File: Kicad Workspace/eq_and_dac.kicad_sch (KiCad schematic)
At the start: 2 parts, among them U3 PCM5242RHBT, U4 TMUX1574PW

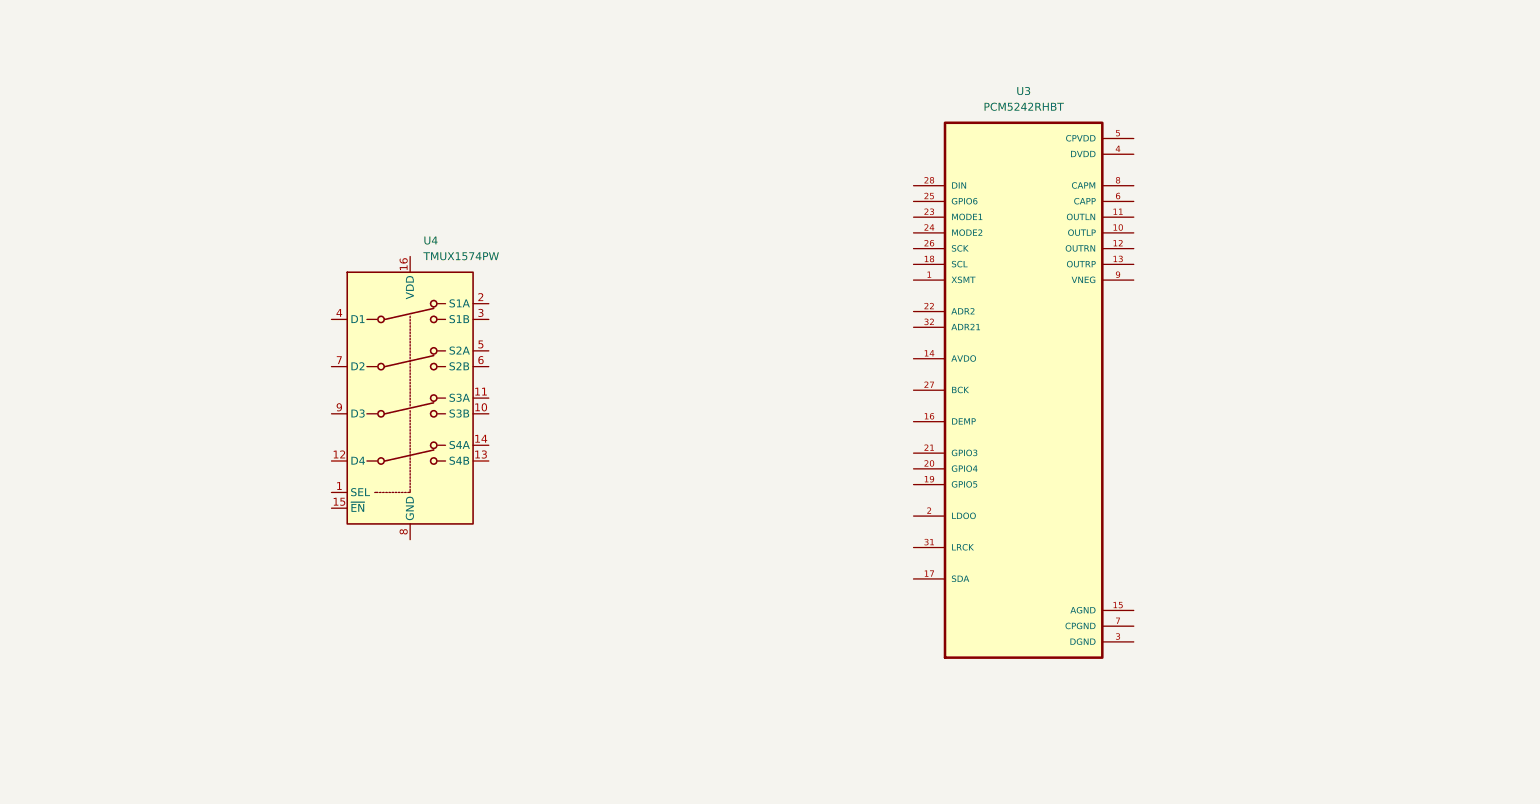
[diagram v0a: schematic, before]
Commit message: feat: MUX + DAC Kicad schematics done
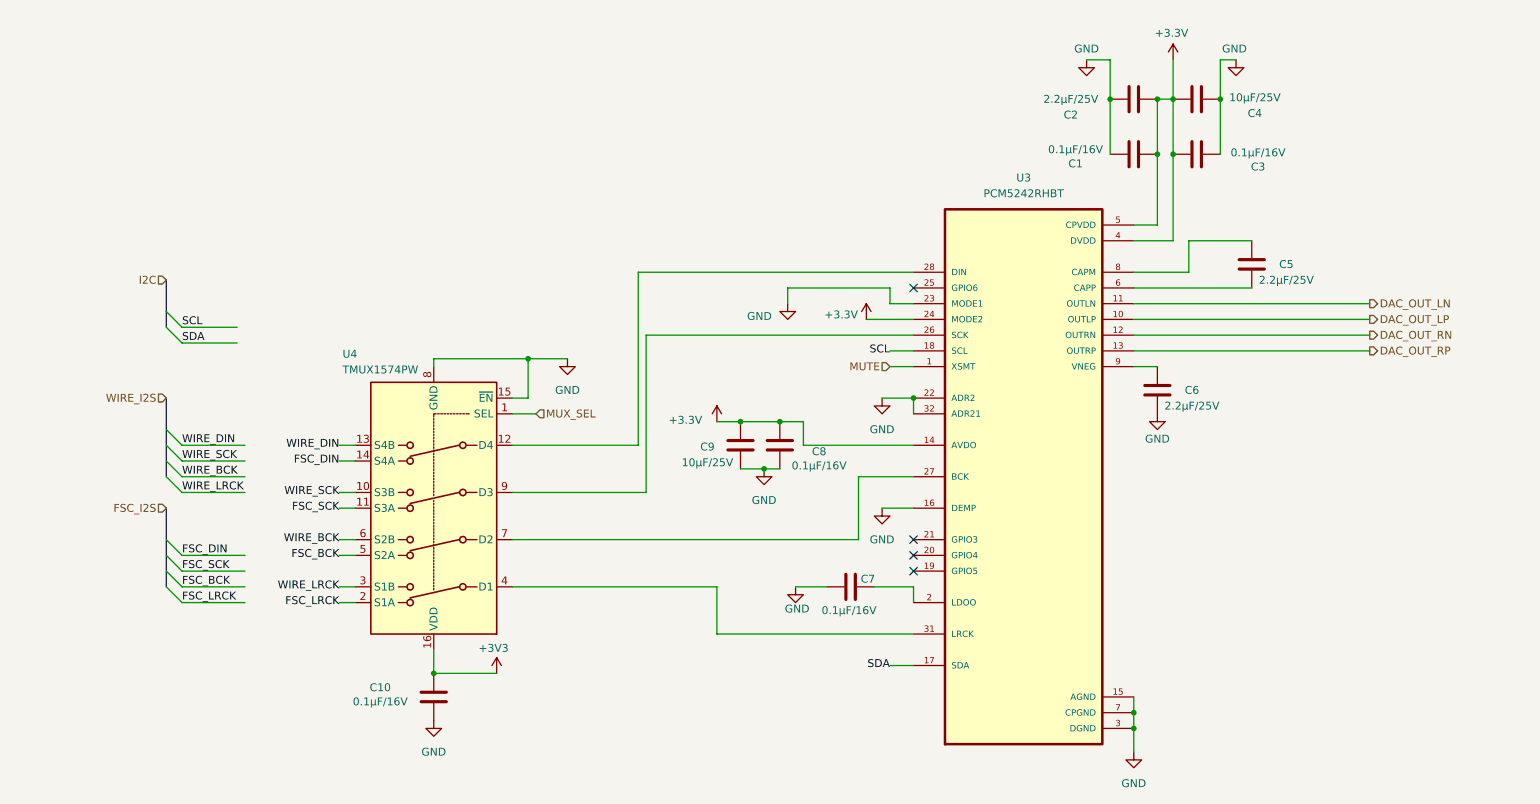
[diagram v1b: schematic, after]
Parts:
- added C1, C10, C3, C7, C8: 0.1µF/16V, Capacitor_SMD:C_0402_1005Metric, symbol Device:C
- added C2, C5, C6: 2.2µF/25V, Capacitor_SMD:C_0805_2012Metric, symbol Device:C
- added C4, C9: 10µF/25V, Capacitor_SMD:C_0805_2012Metric, symbol Device:C
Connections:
- net MUX_SEL: now reaches U4.1 (SEL)
- net WIRE_SCK: now reaches U4.10 (S3B)
- net FSC_SCK: now reaches U4.11 (S3A)
- net at U4.12 (D4): now also U3.28 (DIN)
- net WIRE_DIN: now reaches U4.13 (S4B)
- net FSC_DIN: now reaches U4.14 (S4A)
- net GND: now reaches U4.15 (~{EN})
- net GND: now also U3.15 (AGND), U3.16 (DEMP), U3.22 (ADR2), U3.23 (MODE1), U3.3 (DGND), U3.32 (ADR21), U3.7 (CPGND), U4.8 (GND), C1.1, C10.1, C2.1, C3.2, C4.2, C6.2, C7.1, C8.1, C9.1
- net +3V3: now reaches U4.16 (VDD)
- net +3V3: now also C10.2
- net FSC_LRCK: now reaches U4.2 (S1A)
- net WIRE_LRCK: now reaches U4.3 (S1B)
- net at U4.4 (D1): now also U3.31 (LRCK)
- net FSC_BCK: now reaches U4.5 (S2A)
- net WIRE_BCK: now reaches U4.6 (S2B)
- net at U4.7 (D2): now also U3.27 (BCK)
- net at U4.9 (D3): now also U3.26 (SCK)
- net MUTE: now reaches U3.1 (XSMT)
- net DAC_OUT_LP: now reaches U3.10 (OUTLP)
- net DAC_OUT_LN: now reaches U3.11 (OUTLN)
- net DAC_OUT_RN: now reaches U3.12 (OUTRN)
- net DAC_OUT_RP: now reaches U3.13 (OUTRP)
- net +3.3V: now reaches U3.14 (AVDO)
- net +3.3V: now also U3.24 (MODE2), U3.4 (DVDD), U3.5 (CPVDD), C1.2, C2.2, C3.1, C4.1, C8.2, C9.2
- net SDA: now reaches U3.17 (SDA)
- net SCL: now reaches U3.18 (SCL)
- net at U3.2 (LDOO): now also C7.2
- net at U3.6 (CAPP): now also C5.2
- net at U3.8 (CAPM): now also C5.1
- net at U3.9 (VNEG): now also C6.1
- no-connect marks 0 -> 4
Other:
- moved on the sheet: U3, U4

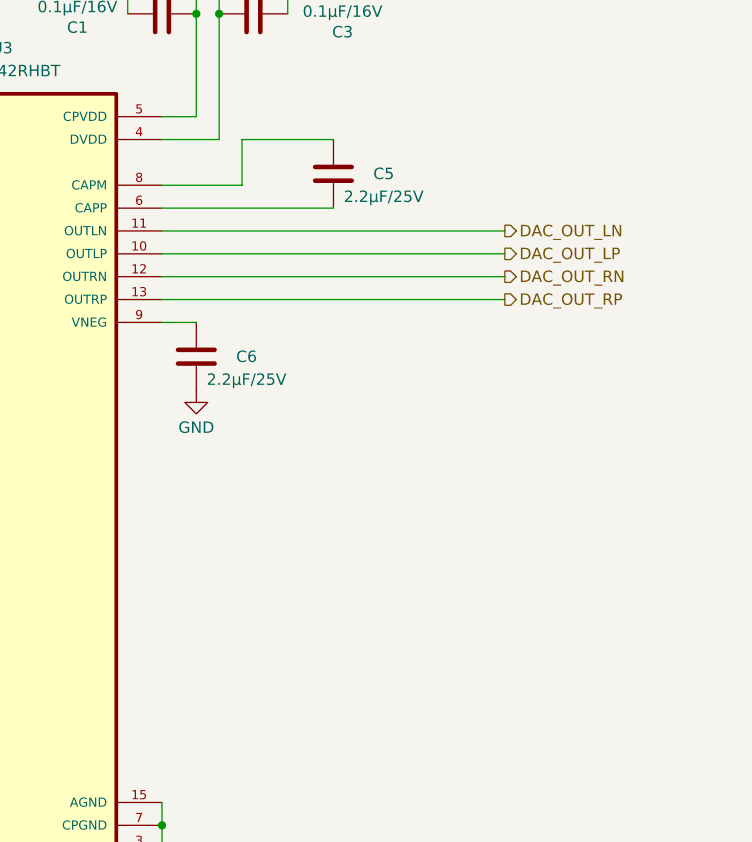
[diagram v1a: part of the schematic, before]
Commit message: feat: filtering analog output
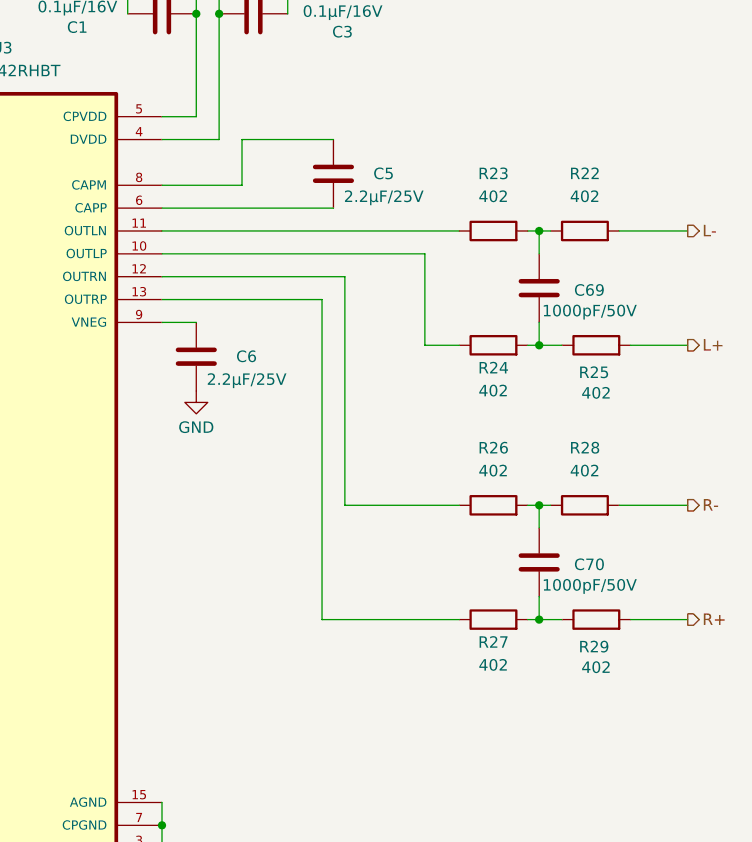
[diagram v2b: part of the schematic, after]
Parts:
- added C69, C70: 1000pF/50V, Capacitor_SMD:C_0201_0603Metric, symbol Device:C
- added R22, R23, R24, R25, R26, R27, R28, R29: 402, Resistor_SMD:R_0201_0603Metric, symbol Device:R
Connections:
- net DAC_OUT_LN: no longer names the net of U3.11 (OUTLN)
- net DAC_OUT_LN: now also R23.1
- net DAC_OUT_LP: no longer names the net of U3.10 (OUTLP)
- net DAC_OUT_LP: now also R24.1
- net DAC_OUT_RN: no longer names the net of U3.12 (OUTRN)
- net DAC_OUT_RN: now also R26.1
- net DAC_OUT_RP: no longer names the net of U3.13 (OUTRP)
- net DAC_OUT_RP: now also R27.1
- new net: C69.2, R22.1, R23.2
- new net: C70.2, R26.2, R28.1
- new net: C69.1, R24.2, R25.1
- new net: C70.1, R27.2, R29.1
- new net L+: R25.2
- new net L-: R22.2
- new net R+: R29.2
- new net R-: R28.2

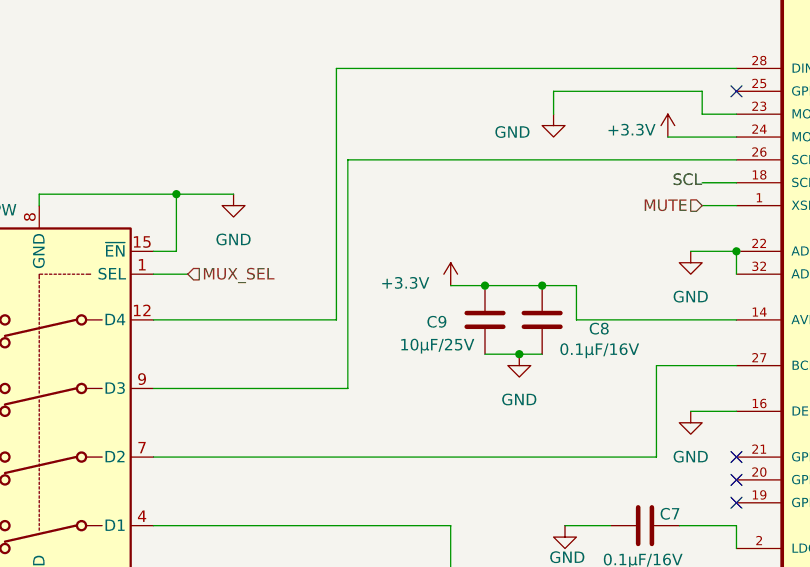
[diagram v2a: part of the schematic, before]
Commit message: fix: split analog 3.3 from digital 3.3
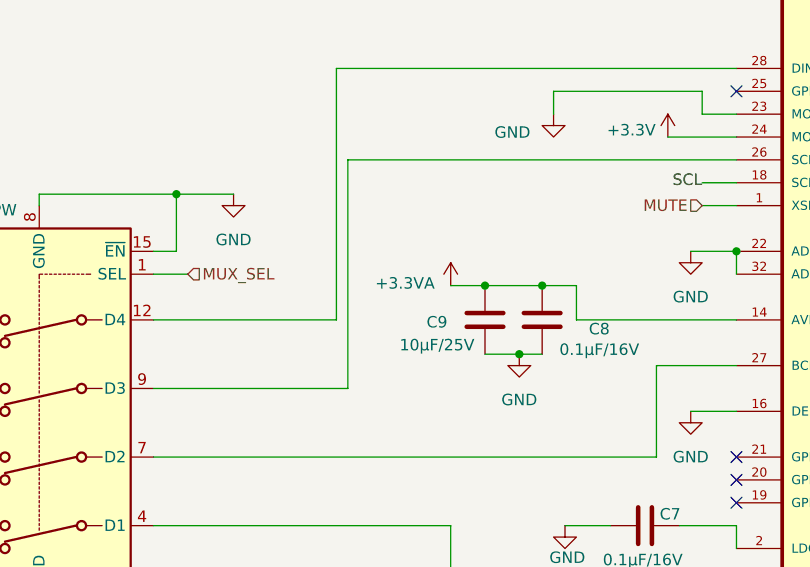
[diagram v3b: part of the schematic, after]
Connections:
- net +3.3V: no longer C8.2, C9.2, U3.14 (AVDO)
- new net +3.3VA: C8.2, C9.2, U3.14 (AVDO)
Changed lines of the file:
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@@
 			)
 		)
-		(property "Value" "+3.3V"
+		(property "Value" "+3.3VA"
 			(at 130.81 93.726 0)
 			(show_name no)

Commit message: feat: schematics almost done, starting to correct compile pb
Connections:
- net FSC_SCK is gone; now on net GND: U4.11 (S3A)
- net WIRE_SCK is gone; now on net GND: U4.10 (S3B)
- net GND: now also U3.26 (SCK), U4.9 (D3)
- net FSC_BCK renamed BT_BCK
- net FSC_DIN renamed BT_DATA
- net FSC_LRCK renamed BT_LRCK
- net WIRE_DIN renamed WIRE_DATA

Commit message: feat: correction work in progress
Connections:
- net SCL renamed I2S.SCL
- net SDA renamed I2S.SDA
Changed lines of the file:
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@@
 	)
 	(bus_entry
-		(at 95.25 54.61)
+		(at 73.66 52.07)
 		(size 2.54 2.54)
 		(stroke
@@
 	)
 	(bus_entry
-		(at 95.25 69.85)
+		(at 73.66 67.31)
 		(size 2.54 2.54)
 		(stroke
@@
 	)
 	(bus_entry
-		(at 95.25 52.07)
+		(at 73.66 49.53)
 		(size 2.54 2.54)
 		(stroke
@@
 	)
 	(bus_entry
-		(at 95.25 72.39)
+		(at 73.66 69.85)
 		(size 2.54 2.54)
 		(stroke
@@
 	)
 	(bus_entry
-		(at 95.25 67.31)
+		(at 73.66 64.77)
 		(size 2.54 2.54)
 		(stroke
@@
 	)
 	(bus_entry
-		(at 95.25 49.53)
+		(at 73.66 46.99)
 		(size 2.54 2.54)
 		(stroke
@@
 	(wire
 		(pts
-			(xy 97.79 72.39) (xy 107.95 72.39)
+			(xy 76.2 69.85) (xy 86.36 69.85)
 		)
 		(stroke
@@
 	(wire
 		(pts
-			(xy 97.79 57.15) (xy 107.95 57.15)
+			(xy 76.2 54.61) (xy 86.36 54.61)
 		)
 		(stroke
@@
 	(wire
 		(pts
-			(xy 97.79 52.07) (xy 107.95 52.07)
-		)
-		(stroke
-			(width 0)
-			(type default)
-		)
-	)
-	(wire
-		(pts
-			(xy 97.79 69.85) (xy 107.95 69.85)
+			(xy 76.2 49.53) (xy 86.36 49.53)
+		)
+		(stroke
+			(width 0)
+			(type default)
+		)
+	)
+	(wire
+		(pts
+			(xy 76.2 67.31) (xy 86.36 67.31)
 		)
 		(stroke
@@
 	(wire
 		(pts
-			(xy 97.79 54.61) (xy 107.95 54.61)
+			(xy 76.2 52.07) (xy 86.36 52.07)
 		)
 		(stroke
@@
 	(wire
 		(pts
-			(xy 97.79 74.93) (xy 107.95 74.93)
+			(xy 76.2 72.39) (xy 86.36 72.39)
 		)
 		(stroke
@@
 	(bus
 		(pts
-			(xy 95.25 59.69) (xy 95.25 72.39)
+			(xy 73.66 57.15) (xy 73.66 69.85)
 		)
 		(stroke
@@
 	(bus
 		(pts
-			(xy 95.25 41.91) (xy 95.25 54.61)
+			(xy 73.66 39.37) (xy 73.66 52.07)
 		)
 		(stroke
@@
 		)
 	)
-	(label "SDA"
+	(label "WIRE_LRCK"
+		(at 86.36 54.61 0)
+		(effects
+			(font
+				(size 1.27 1.27)
+				(thickness 0.1588)
+			)
+			(justify left bottom)
+		)
+	)
+	(label "I2S.SDA"
 		(at 163.83 133.35 180)
 		(effects
@@
 		)
 	)
-	(label "WIRE_LRCK"
-		(at 97.79 57.15 0)
-		(effects
-			(font
-				(size 1.27 1.27)
-				(thickness 0.1588)
-			)
-			(justify left bottom)
-		)
-	)
 	(label "BT_LRCK"
 		(at 74.93 123.19 180)
@@
 		)
 	)
-	(label "WIRE_BCK"
-		(at 97.79 54.61 0)
+	(label "BT_BCK"
+		(at 76.2 69.85 0)
 		(effects
 			(font
@@
 		)
 	)
-	(label "BT_BCK"
-		(at 97.79 72.39 0)
-		(effects
-			(font
-				(size 1.27 1.27)
-				(thickness 0.1588)
-			)
-			(justify left bottom)
-		)
-	)
-	(label "SDA"
+	(label "I2S.SDA"
 		(at 127 40.64 180)
 		(effects
@@
 		)
 	)
-	(label "SCL"
+	(label "WIRE_DATA"
+		(at 86.36 49.53 0)
+		(effects
+			(font
+				(size 1.27 1.27)
+				(thickness 0.1588)
+			)
+			(justify left bottom)
+		)
+	)
+	(label "I2S.SCL"
 		(at 163.83 82.55 180)
 		(effects
@@
 		)
 	)
+	(label "WIRE_BCK"
+		(at 86.36 52.07 0)
+		(effects
+			(font
+				(size 1.27 1.27)
+				(thickness 0.1588)
+			)
+			(justify left bottom)
+		)
+	)
 	(label "BT_DATA"
-		(at 97.79 69.85 0)
+		(at 76.2 67.31 0)
 		(effects
 			(font
@@
 		)
 	)
-	(label "WIRE_DATA"
-		(at 97.79 52.07 0)
+	(label "BT_LRCK"
+		(at 76.2 72.39 0)
 		(effects
 			(font
@@
 		)
 	)
-	(label "BT_LRCK"
-		(at 97.79 74.93 0)
-		(effects
-			(font
-				(size 1.27 1.27)
-				(thickness 0.1588)
-			)
-			(justify left bottom)
-		)
-	)
-	(label "SCL"
+	(label "I2S.SCL"
 		(at 127 36.83 180)
 		(effects
@@
 	(hierarchical_label "WIRE_I2S{WIRE_DATA WIRE_BCK WIRE_LRCK}"
 		(shape input)
-		(at 95.25 41.91 180)
+		(at 73.66 39.37 180)
 		(effects
 			(font
@@
 	(hierarchical_label "BT_I2S{BT_DATA BT_BCK BT_LRCK}"
 		(shape input)
-		(at 95.25 59.69 180)
-		(effects
-			(font
+		(at 73.66 57.15 180)
+		(effects
+			(font

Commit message: project update
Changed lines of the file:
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@@
 		(property "Footprint" "PCM5242RHBT:IC_ADS125H01IRHBT"
 			(at 185.42 102.87 0)
-			(hide yes)
 			(show_name no)
 			(do_not_autoplace no)

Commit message: fix: Bus fix with correct syntax
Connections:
- net +3V3 is gone; now on net +3.3V: C10.2, U4.16 (VDD)
- net BT_BCK renamed BT_I2S.BCK
- net BT_DATA renamed BT_I2S.DATA
- net BT_LRCK renamed BT_I2S.LRCK
- net I2S.SCL renamed I2C.SCL
- net I2S.SDA renamed I2C.SDA
- net WIRE_BCK renamed WIRE_I2S.BCK
- net WIRE_DATA renamed WIRE_I2S.DATA
- net WIRE_LRCK renamed WIRE_I2S.LRCK
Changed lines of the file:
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@@
 	(wire
 		(pts
-			(xy 76.2 69.85) (xy 86.36 69.85)
-		)
-		(stroke
-			(width 0)
-			(type default)
-		)
-	)
-	(wire
-		(pts
 			(xy 245.11 74.93) (xy 246.38 74.93)
 		)
@@
 	(wire
 		(pts
-			(xy 76.2 49.53) (xy 86.36 49.53)
-		)
-		(stroke
-			(width 0)
-			(type default)
-		)
-	)
-	(wire
-		(pts
 			(xy 76.2 67.31) (xy 86.36 67.31)
 		)
@@
 	(wire
 		(pts
+			(xy 76.2 69.85) (xy 86.36 69.85)
+		)
+		(stroke
+			(width 0)
+			(type default)
+		)
+	)
+	(wire
+		(pts
 			(xy 74.93 113.03) (xy 77.47 113.03)
 		)
@@
 	(wire
 		(pts
+			(xy 76.2 49.53) (xy 86.36 49.53)
+		)
+		(stroke
+			(width 0)
+			(type default)
+		)
+	)
+	(wire
+		(pts
 			(xy 245.11 105.41) (xy 245.11 107.95)
 		)
@@
 	(wire
 		(pts
-			(xy 76.2 72.39) (xy 86.36 72.39)
+			(xy 254 74.93) (xy 261.62 74.93)
 		)
 		(stroke
@@
 	(wire
 		(pts
-			(xy 254 74.93) (xy 261.62 74.93)
+			(xy 217.17 35.56) (xy 217.17 41.91)
 		)
 		(stroke
@@
 	(wire
 		(pts
-			(xy 217.17 35.56) (xy 217.17 41.91)
+			(xy 254 105.41) (xy 261.62 105.41)
 		)
 		(stroke
@@
 	(wire
 		(pts
-			(xy 254 105.41) (xy 261.62 105.41)
+			(xy 232.41 87.63) (xy 236.22 87.63)
 		)
 		(stroke
@@
 	(wire
 		(pts
-			(xy 232.41 87.63) (xy 236.22 87.63)
+			(xy 76.2 72.39) (xy 86.36 72.39)
 		)
 		(stroke
@@
 		)
 	)
-	(label "WIRE_LRCK"
+	(label "WIRE_I2S.LRCK"
 		(at 86.36 54.61 0)
 		(effects
@@
 		)
 	)
-	(label "I2S.SDA"
+	(label "I2C.SDA"
 		(at 163.83 133.35 180)
 		(effects
@@
 		)
 	)
-	(label "BT_BCK"
+	(label "BT_I2S.BCK"
 		(at 74.93 115.57 180)
 		(effects
@@
 		)
 	)
-	(label "BT_LRCK"
+	(label "BT_I2S.LRCK"
 		(at 74.93 123.19 180)
 		(effects
@@
 		)
 	)
-	(label "BT_BCK"
-		(at 76.2 69.85 0)
+	(label "BT_I2S.BCK"
+		(at 86.36 69.85 0)
 		(effects
 			(font
@@
 		)
 	)
-	(label "I2S.SDA"
+	(label "I2C.SDA"
 		(at 127 40.64 180)
 		(effects
@@
 		)
 	)
-	(label "WIRE_DATA"
+	(label "WIRE_I2S.DATA"
 		(at 74.93 97.79 180)
 		(effects
@@
 		)
 	)
-	(label "WIRE_DATA"
+	(label "WIRE_I2S.DATA"
 		(at 86.36 49.53 0)
 		(effects
@@
 		)
 	)
-	(label "I2S.SCL"
+	(label "I2C.SCL"
 		(at 163.83 82.55 180)
 		(effects
@@
 		)
 	)
-	(label "WIRE_LRCK"
+	(label "WIRE_I2S.LRCK"
 		(at 74.93 120.65 180)
 		(effects
@@
 		)
 	)
-	(label "WIRE_BCK"
+	(label "WIRE_I2S.BCK"
 		(at 74.93 113.03 180)
 		(effects
@@
 		)
 	)
-	(label "BT_DATA"
+	(label "BT_I2S.DATA"
 		(at 74.93 100.33 180)
 		(effects
@@
 		)
 	)
-	(label "WIRE_BCK"
+	(label "WIRE_I2S.BCK"
 		(at 86.36 52.07 0)
 		(effects
@@
 		)
 	)
-	(label "BT_DATA"
-		(at 76.2 67.31 0)
+	(label "BT_I2S.DATA"
+		(at 86.36 67.31 0)
 		(effects
 			(font
@@
 		)
 	)
-	(label "BT_LRCK"
-		(at 76.2 72.39 0)
+	(label "BT_I2S.LRCK"
+		(at 86.36 72.39 0)
 		(effects
 			(font
@@
 		)
 	)
-	(label "I2S.SCL"
+	(label "I2C.SCL"
 		(at 127 36.83 180)
 		(effects
@@
 		)
 	)
-	(hierarchical_label "WIRE_I2S{WIRE_DATA WIRE_BCK WIRE_LRCK}"
+	(hierarchical_label "WIRE_I2S{DATA BCK LRCK}"
 		(shape input)
 		(at 73.66 39.37 180)
@@
 		)
 	)
-	(hierarchical_label "BT_I2S{BT_DATA BT_BCK BT_LRCK}"
+	(hierarchical_label "BT_I2S{DATA BCK LRCK}"
 		(shape input)
 		(at 73.66 57.15 180)
@@
 	)
 	(symbol
-		(lib_id "power:+3V3")
-		(at 100.33 134.62 0)
-		(unit 1)
-		(body_style 1)
-		(exclude_from_sim no)
-		(in_bom yes)
-		(on_board yes)
-		(in_pos_files yes)
-		(dnp no)
-		(property "Reference" "#PWR02"
-			(at 100.33 138.43 0)
-			(hide yes)
-			(show_name no)
-			(do_not_autoplace no)
-			(effects
-				(font
-					(size 1.27 1.27)
-				)
-			)
-		)
-		(property "Value" "+3V3"
-			(at 99.822 130.556 0)
-			(show_name no)
-			(do_not_autoplace no)
-			(effects
-				(font
-					(size 1.27 1.27)
-					(color 255 0 28 1)
-				)
-			)
-		)
-		(property "Footprint" ""
-			(at 100.33 134.62 0)
-			(hide yes)
-			(show_name no)
-			(do_not_autoplace no)
-			(effects
-				(font
-					(size 1.27 1.27)
-				)
-			)
-		)
-		(property "Datasheet" ""
-			(at 100.33 134.62 0)
-			(hide yes)
-			(show_name no)
-			(do_not_autoplace no)
-			(effects
-				(font
-					(size 1.27 1.27)
-				)
-			)
-		)
-		(property "Description" "Power symbol creates a global label with name \"+3V3\""
-			(at 100.33 134.62 0)
-			(hide yes)
-			(show_name no)
-			(do_not_autoplace no)
-			(effects
-				(font
-					(size 1.27 1.27)
-				)
-			)
-		)
-		(pin "1"
-		)
-		(instances
-			(project "Kicad Workspace"
-				(path "/7c7afbb1-f4ab-42aa-9bad-41afd809eff4/601c925f-039e-4bfe-8f5f-c430ecebffaa"
-					(reference "#PWR02")
-					(unit 1)
-				)
-			)
-		)
-	)
-	(symbol
 		(lib_id "Device:R")
 		(at 251.46 118.11 90)
@@
 		(property "Footprint" "PCM5242RHBT:IC_ADS125H01IRHBT"
 			(at 185.42 102.87 0)
+			(hide yes)
 			(show_name no)
 			(do_not_autoplace no)
@@
 					(unit 1)
 				)
+			)
+		)
+	)
+	(symbol
+		(lib_id "power:+3.3V")
+		(at 100.33 134.62 0)
+		(unit 1)
+		(body_style 1)
+		(exclude_from_sim no)
+		(in_bom yes)
+		(on_board yes)
+		(in_pos_files yes)
+		(dnp no)
+		(property "Reference" "#PWR088"
+			(at 100.33 138.43 0)
+			(hide yes)
+			(show_name no)
+			(do_not_autoplace no)
+			(effects
+				(font
+					(size 1.27 1.27)
+				)
+			)
+		)
+		(property "Value" "+3.3V"
+			(at 100.076 130.302 0)
+			(show_name no)
+			(do_not_autoplace no)
+			(effects
+				(font
+					(size 1.27 1.27)
+				)
+			)
+		)
+		(property "Footprint" ""
+			(at 100.33 134.62 0)
+			(hide yes)
+			(show_name no)
+			(do_not_autoplace no)
+			(effects
+				(font
+					(size 1.27 1.27)
+				)
+			)
+		)
+		(property "Datasheet" ""
+			(at 100.33 134.62 0)
+			(hide yes)
+			(show_name no)
+			(do_not_autoplace no)
+			(effects
+				(font
+					(size 1.27 1.27)
+				)
+			)
+		)
+		(property "Description" "Power symbol creates a global label with name \"+3.3V\""
+			(at 100.33 134.62 0)
+			(hide yes)
+			(show_name no)
+			(do_not_autoplace no)
+			(effects
+				(font
+					(size 1.27 1.27)
+				)
+			)
+		)
+		(pin "1"
+		)
+		(instances
+			(project "Kicad Workspace"
+				(path "/7c7afbb1-f4ab-42aa-9bad-41afd809eff4/601c925f-039e-4bfe-8f5f-c430ecebffaa"
+					(reference "#PWR088")
+					(unit 1)
+				)
